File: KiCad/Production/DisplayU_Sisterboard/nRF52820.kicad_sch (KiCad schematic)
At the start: 20 parts, among them X1 32MHz ±40 ppm

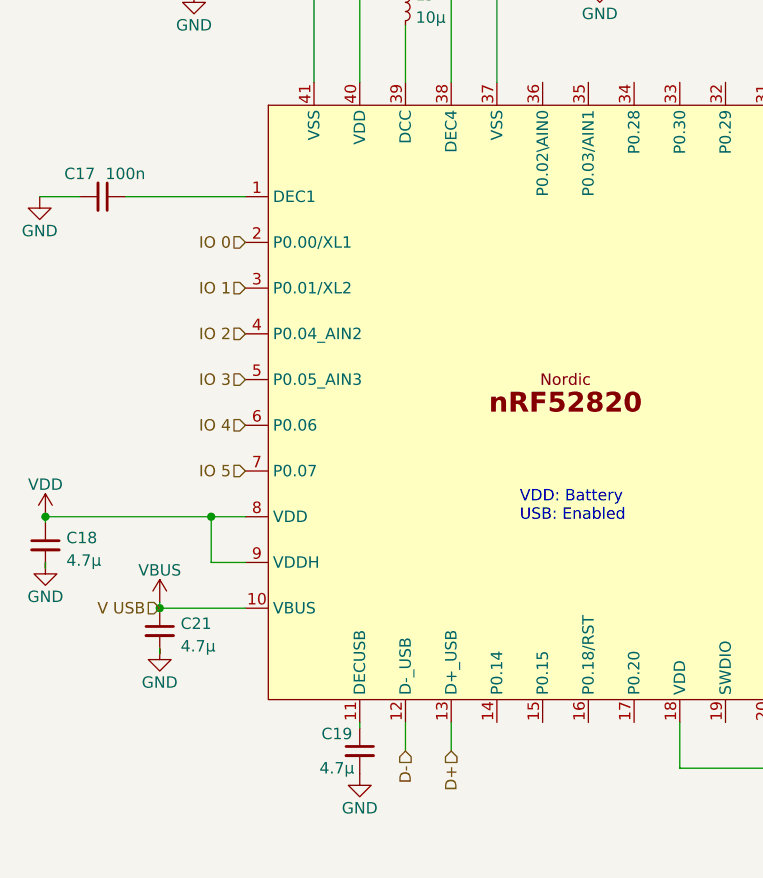
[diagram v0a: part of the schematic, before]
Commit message: Microcontroller integration (almost done)
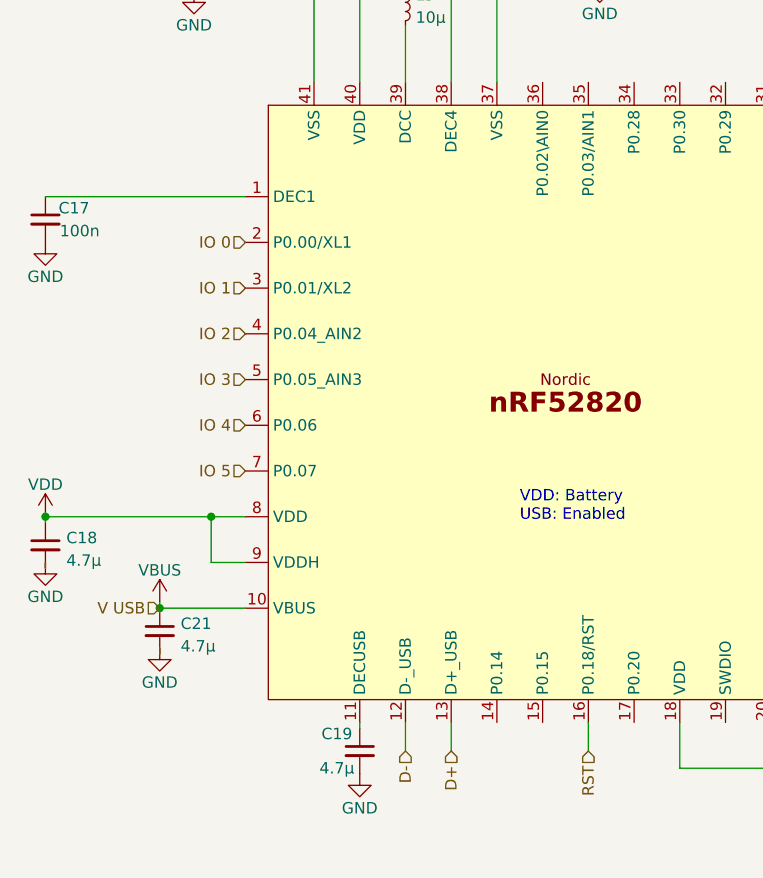
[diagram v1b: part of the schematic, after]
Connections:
- net RST: now reaches U1.16 (P0.18/RST)
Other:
- moved on the sheet: C17
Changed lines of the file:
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@@
     (stroke (width 0) (type default))
   )
-  (wire (pts (xy 124.46 73.66) (xy 111.125 73.66))
+  (wire (pts (xy 124.46 73.66) (xy 102.235 73.66))
     (stroke (width 0) (type default))
   )
@@
     (stroke (width 0) (type default))
   )
+  (wire (pts (xy 162.56 132.08) (xy 162.56 135.255))
+    (stroke (width 0) (type default))
+  )
   (wire (pts (xy 132.08 50.8) (xy 118.745 50.8))
     (stroke (width 0) (type default))
@@
   )
   (wire (pts (xy 114.935 119.38) (xy 114.935 118.745))
-    (stroke (width 0) (type default))
-  )
-  (wire (pts (xy 106.045 73.66) (xy 101.6 73.66))
     (stroke (width 0) (type default))
   )
@@
   )
   (hierarchical_label "D-" (shape input) (at 142.24 135.255 270) (fields_autoplaced)
+    (effects (font (size 1.27 1.27)) (justify right))
+  )
+  (hierarchical_label "RST" (shape input) (at 162.56 135.255 270) (fields_autoplaced)
     (effects (font (size 1.27 1.27)) (justify right))
   )
@@
     )
   )
-  (symbol (lib_id "power:GND") (at 101.6 73.66 0) (unit 1)
-    (in_bom yes) (on_board yes) (dnp no)
-    (property "Reference" "#PWR015" (at 101.6 80.01 0)
-      (effects (font (size 1.27 1.27)) hide)
-    )
-    (property "Value" "GND" (at 101.6 77.47 0)
-      (effects (font (size 1.27 1.27)))
-    )
-    (property "Footprint" "" (at 101.6 73.66 0)
-      (effects (font (size 1.27 1.27)) hide)
-    )
-    (property "Datasheet" "" (at 101.6 73.66 0)
+  (symbol (lib_id "power:GND") (at 102.235 78.74 0) (unit 1)
+    (in_bom yes) (on_board yes) (dnp no)
+    (property "Reference" "#PWR015" (at 102.235 85.09 0)
+      (effects (font (size 1.27 1.27)) hide)
+    )
+    (property "Value" "GND" (at 102.235 82.55 0)
+      (effects (font (size 1.27 1.27)))
+    )
+    (property "Footprint" "" (at 102.235 78.74 0)
+      (effects (font (size 1.27 1.27)) hide)
+    )
+    (property "Datasheet" "" (at 102.235 78.74 0)
       (effects (font (size 1.27 1.27)) hide)
     )
@@
     )
   )
-  (symbol (lib_id "Device:C_Small") (at 108.585 73.66 270) (unit 1)
-    (in_bom yes) (on_board yes) (dnp no)
-    (property "Reference" "C17" (at 106.045 71.12 90)
-      (effects (font (size 1.27 1.27)))
-    )
-    (property "Value" "100n" (at 111.125 71.12 90)
-      (effects (font (size 1.27 1.27)))
-    )
-    (property "Footprint" "" (at 108.585 73.66 0)
-      (effects (font (size 1.27 1.27)) hide)
-    )
-    (property "Datasheet" "~" (at 108.585 73.66 0)
-      (effects (font (size 1.27 1.27)) hide)
-    )
+  (symbol (lib_id "Device:C_Small") (at 102.235 76.2 0) (unit 1)
+    (in_bom yes) (on_board yes) (dnp no)
+    (property "Reference" "C17" (at 105.41 74.93 0)
+      (effects (font (size 1.27 1.27)))
+    )
+    (property "Value" "100n" (at 106.045 77.47 0)
+      (effects (font (size 1.27 1.27)))
+    )
+    (property "Footprint" "" (at 102.235 76.2 0)
+      (effects (font (size 1.27 1.27)) hide)
+    )
+    (property "Datasheet" "~" (at 102.235 76.2 0)
+      (effects (font (size 1.27 1.27)) hide)
+    )

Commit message: Display U is like 99% finished
- BMS Chips prob not needed
- LDO Chip prob not needed
- Final touches
> Start on routing
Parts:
- C1, C15, C16, C17, C18, C19, C2, C20, C21, C3, C4, C5, C6, C7: footprint (none) -> Capacitor_SMD:C_0603_1608Metric
- U1: footprint (none) -> Package_DFN_QFN:QFN-40-1EP_5x5mm_P0.4mm_EP3.8x3.8mm
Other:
- note added: "Datasheet"
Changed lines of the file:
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@@
     (stroke (width 0) (type default))
+  )
+  (text "Datasheet" (at 193.675 67.945 0)
+    (effects (font (size 1.27 1.27)) (justify left bottom) (href "https://infocenter.nordicsemi.com/index.jsp?topic=%2Fps_nrf52820%2Fordering_info.html"))
   )
   (text "VDD: Battery\nUSB: Enabled\n" (at 154.94 109.855 0)
@@
       (effects (font (size 1.27 1.27)))
     )
-    (property "Footprint" "" (at 215.9 88.9 0)
+    (property "Footprint" "Capacitor_SMD:C_0603_1608Metric" (at 215.9 88.9 0)
       (effects (font (size 1.27 1.27)) hide)
     )
@@
       (effects (font (size 1.27 1.27)))
     )
-    (property "Footprint" "" (at 215.9 78.74 0)
+    (property "Footprint" "Capacitor_SMD:C_0603_1608Metric" (at 215.9 78.74 0)
       (effects (font (size 1.27 1.27)) hide)
     )
@@
   )
   (symbol (lib_id "NRF:nRF52820") (at 127 63.5 0) (unit 1)
-    (in_bom yes) (on_board yes) (dnp no) (fields_autoplaced)
-    (property "Reference" "U1" (at 194.7643 69.132 0)
+    (in_bom yes) (on_board yes) (dnp no)
+    (property "Reference" "U1" (at 194.945 64.77 0)
       (effects (font (size 1.27 1.27)))
     )
@@
       (effects (font (size 1.27 1.27)))
     )
-    (property "Footprint" "" (at 127 66.04 0)
+    (property "Footprint" "Package_DFN_QFN:QFN-40-1EP_5x5mm_P0.4mm_EP3.8x3.8mm" (at 127 66.04 0)
       (effects (font (size 1.27 1.27)) hide)
     )
@@
       (effects (font (size 1.27 1.27)) (justify left))
     )
-    (property "Footprint" "" (at 118.745 47.625 0)
+    (property "Footprint" "Capacitor_SMD:C_0603_1608Metric" (at 118.745 47.625 0)
       (effects (font (size 1.27 1.27)) hide)
     )
@@
       (effects (font (size 1.27 1.27)) (justify left))
     )
-    (property "Footprint" "" (at 205.74 139.7 0)
+    (property "Footprint" "Capacitor_SMD:C_0603_1608Metric" (at 205.74 139.7 0)
       (effects (font (size 1.27 1.27)) hide)
     )
@@
       (effects (font (size 1.27 1.27)) (justify left))
     )
-    (property "Footprint" "" (at 114.935 121.92 0)
+    (property "Footprint" "Capacitor_SMD:C_0603_1608Metric" (at 114.935 121.92 0)
       (effects (font (size 1.27 1.27)) hide)
     )
@@
       (effects (font (size 1.27 1.27)) (justify left))
     )
-    (property "Footprint" "" (at 157.48 46.99 0)
+    (property "Footprint" "Capacitor_SMD:C_0603_1608Metric" (at 157.48 46.99 0)
       (effects (font (size 1.27 1.27)) hide)
     )
@@
       (effects (font (size 1.27 1.27)) (justify left))
     )
-    (property "Footprint" "" (at 222.885 64.135 0)
+    (property "Footprint" "Capacitor_SMD:C_0603_1608Metric" (at 222.885 64.135 0)
       (effects (font (size 1.27 1.27)) hide)
     )
@@
       (effects (font (size 1.27 1.27)) hide)
     )
-    (property "Footprint" "" (at 215.9 83.82 0)
+    (property "Footprint" "Capacitor_SMD:C_0603_1608Metric" (at 215.9 83.82 0)
       (effects (font (size 1.27 1.27)) hide)
     )
@@
       (effects (font (size 1.27 1.27)) (justify left))
     )
-    (property "Footprint" "" (at 217.17 106.68 0)
+    (property "Footprint" "Capacitor_SMD:C_0603_1608Metric" (at 217.17 106.68 0)
       (effects (font (size 1.27 1.27)) hide)
     )
@@
       (effects (font (size 1.27 1.27)))
     )
-    (property "Footprint" "" (at 102.235 76.2 0)
+    (property "Footprint" "Capacitor_SMD:C_0603_1608Metric" (at 102.235 76.2 0)
       (effects (font (size 1.27 1.27)) hide)
     )
@@
       (effects (font (size 1.27 1.27)))
     )
-    (property "Footprint" "" (at 137.16 135.255 0)
+    (property "Footprint" "Capacitor_SMD:C_0603_1608Metric" (at 137.16 135.255 0)
       (effects (font (size 1.27 1.27)) hide)
     )
@@
       (effects (font (size 1.27 1.27)) (justify left))
     )
-    (property "Footprint" "" (at 205.105 106.68 0)
+    (property "Footprint" "Capacitor_SMD:C_0603_1608Metric" (at 205.105 106.68 0)
       (effects (font (size 1.27 1.27)) hide)
     )
@@
       (effects (font (size 1.27 1.27)) (justify left))
     )
-    (property "Footprint" "" (at 102.235 112.395 0)
+    (property "Footprint" "Capacitor_SMD:C_0603_1608Metric" (at 102.235 112.395 0)
       (effects (font (size 1.27 1.27)) hide)
     )
@@
       (effects (font (size 1.27 1.27)) (justify left))
     )
-    (property "Footprint" "" (at 163.83 46.99 0)
-      (effects (font (size 1.27 1.27)) hide)
-    )
+    (property "Footprint" "Capacitor_SMD:C_0603_1608Metric" (at 163.83 46.99 0)
+      (effects (font (size 1.27 1.27)) hide)
+    )

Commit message: Schematic is done
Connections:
- net IO 6: now reaches U1.31 (P0.08)
- net D+ renamed DATA+
- net D- renamed DATA-
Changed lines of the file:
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@@
     (effects (font (size 1.27 1.27)) (justify left bottom))
+  )
+  (global_label "DATA+" (shape input) (at 147.32 135.255 270) (fields_autoplaced)
+    (effects (font (size 1.27 1.27)) (justify right))
+    (property "Intersheetrefs" "${INTERSHEET_REFS}" (at 147.32 143.4138 90)
+      (effects (font (size 1.27 1.27)) (justify right) hide)
+    )
+  )
+  (global_label "GND" (shape input) (at 18.415 20.32 0) (fields_autoplaced)
+    (effects (font (size 1.27 1.27)) (justify left))
+    (property "Intersheetrefs" "${INTERSHEET_REFS}" (at 24.9732 20.32 0)
+      (effects (font (size 1.27 1.27)) (justify left) hide)
+    )
+  )
+  (global_label "DATA-" (shape input) (at 142.24 135.255 270) (fields_autoplaced)
+    (effects (font (size 1.27 1.27)) (justify right))
+    (property "Intersheetrefs" "${INTERSHEET_REFS}" (at 142.24 142.9088 90)
+      (effects (font (size 1.27 1.27)) (justify right) hide)
+    )
+  )
+  (global_label "VBUS" (shape input) (at 114.935 119.38 180) (fields_autoplaced)
+    (effects (font (size 1.27 1.27)) (justify right))
+    (property "Intersheetrefs" "${INTERSHEET_REFS}" (at 107.8842 119.38 0)
+      (effects (font (size 1.27 1.27)) (justify right) hide)
+    )
   )
   (hierarchical_label "RF" (shape input) (at 234.95 104.14 0) (fields_autoplaced)
@@
     (effects (font (size 1.27 1.27)) (justify right))
   )
-  (hierarchical_label "D+" (shape input) (at 147.32 135.255 270) (fields_autoplaced)
-    (effects (font (size 1.27 1.27)) (justify right))
-  )
-  (hierarchical_label "GND" (shape input) (at 118.745 50.8 180) (fields_autoplaced)
-    (effects (font (size 1.27 1.27)) (justify right))
-  )
-  (hierarchical_label "V USB" (shape input) (at 114.935 119.38 180) (fields_autoplaced)
-    (effects (font (size 1.27 1.27)) (justify right))
-  )
   (hierarchical_label "IO 2" (shape input) (at 124.46 88.9 180) (fields_autoplaced)
     (effects (font (size 1.27 1.27)) (justify right))
@@
     (effects (font (size 1.27 1.27)) (justify right))
   )
-  (hierarchical_label "D-" (shape input) (at 142.24 135.255 270) (fields_autoplaced)
-    (effects (font (size 1.27 1.27)) (justify right))
+  (hierarchical_label "IO 6" (shape input) (at 182.88 60.96 90) (fields_autoplaced)
+    (effects (font (size 1.27 1.27)) (justify left))
   )
   (hierarchical_label "RST" (shape input) (at 162.56 135.255 270) (fields_autoplaced)
@@
         )
       )
+    )
+  )
+  (symbol (lib_id "power:GND") (at 18.415 20.32 0) (unit 1)
+    (in_bom yes) (on_board yes) (dnp no)
+    (property "Reference" "#PWR049" (at 18.415 26.67 0)
+      (effects (font (size 1.27 1.27)) hide)
+    )
+    (property "Value" "GND" (at 18.415 24.13 0)
+      (effects (font (size 1.27 1.27)))
+    )
+    (property "Footprint" "" (at 18.415 20.32 0)
+      (effects (font (size 1.27 1.27)) hide)
+    )
+    (property "Datasheet" "" (at 18.415 20.32 0)
+      (effects (font (size 1.27 1.27)) hide)
+    )
+    (pin "1")
+    (instances
+      (project "DisplayU_Sisterboard"
+        (path "/19c7c935-33c8-4c59-9a5d-d605e15c31a3/25a7bd83-bec9-4f3f-8272-59937481b0db/21567c23-4b19-440e-b334-053946d84a03"
+          (reference "#PWR049") (unit 1)
+        )
+        (path "/19c7c935-33c8-4c59-9a5d-d605e15c31a3/25a7bd83-bec9-4f3f-8272-59937481b0db"
+          (reference "#PWR026") (unit 1)
+        )
+      )

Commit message: Routing
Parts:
- added F?: 04941.25NRHF, Fuse:Fuse_0603_1608Metric, symbol Device:Fuse
- L1, L2, L3, L4: footprint (none) -> Inductor_SMD:L_0603_1608Metric
- X1: footprint (none) -> Crystal:Crystal_SMD_SeikoEpson_FA128-4Pin_2.0x1.6mm
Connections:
- net VDD: now also F?.2; no longer U1.40 (VDD)
- net X1+: now reaches C6.1, U1.29 (XC2), X1.2
- net X1-: now reaches C7.1, U1.28 (XC1), X1.1
- new net: F?.1, U1.40 (VDD)
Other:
- note added: "Nordic nRFxx Implementation Battery powered + USB -Sam Dilmaghanian"
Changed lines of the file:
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@@
   (junction (at 222.885 60.96) (diameter 0) (color 0 0 0 0)
   )
-  (wire (pts (xy 118.745 44.45) (xy 137.16 44.45))
-    (stroke (width 0) (type default))
-  )
   (wire (pts (xy 205.74 137.16) (xy 205.74 136.525))
     (stroke (width 0) (type default))
@@
     (stroke (width 0) (type default))
   )
+  (wire (pts (xy 137.16 55.372) (xy 137.16 60.96))
+    (stroke (width 0) (type default))
+  )
   (wire (pts (xy 118.745 50.165) (xy 118.745 50.8))
     (stroke (width 0) (type default))
@@
     (stroke (width 0) (type default))
   )
-  (wire (pts (xy 137.16 44.45) (xy 137.16 60.96))
-    (stroke (width 0) (type default))
-  )
   (wire (pts (xy 120.65 114.3) (xy 120.65 109.22))
     (stroke (width 0) (type default))
@@
     (stroke (width 0) (type default))
   )
+  (wire (pts (xy 137.16 44.45) (xy 118.745 44.45))
+    (stroke (width 0) (type default))
+  )
   (wire (pts (xy 195.58 78.74) (xy 197.485 78.74))
     (stroke (width 0) (type default))
@@
     (stroke (width 0) (type default))
   )
+  (wire (pts (xy 137.16 47.752) (xy 137.16 44.45))
+    (stroke (width 0) (type default))
+  )
   (wire (pts (xy 195.58 99.06) (xy 202.565 99.06))
     (stroke (width 0) (type default))
@@
     (stroke (width 0) (type default))
   )
+  (text "Nordic nRFxx Implementation\nBattery powered + USB\n-Sam Dilmaghanian"
+    (at 179.07 173.99 0)
+    (effects (font (size 1.27 1.27)) (justify left bottom))
+  )
   (text "Datasheet" (at 193.675 67.945 0)
-    (effects (font (size 1.27 1.27)) (justify left bottom) (href "https://infocenter.nordicsemi.com/index.jsp?topic=%2Fps_nrf52820%2Fordering_info.html"))
+    (effects (font (size 1.27 1.27)) (justify left bottom) (href "https://infocenter.nordicsemi.com/pdf/nRF52820_PS_v1.3.pdf"))
   )
   (text "VDD: Battery\nUSB: Enabled\n" (at 154.94 109.855 0)
+    (effects (font (size 1.27 1.27)) (justify left bottom))
+  )
+  (label "X1-" (at 206.248 83.82 270) (fields_autoplaced)
+    (effects (font (size 1.27 1.27)) (justify right bottom))
+  )
+  (label "D-" (at 142.24 133.223 270) (fields_autoplaced)
+    (effects (font (size 1.27 1.27)) (justify right bottom))
+  )
+  (label "D+" (at 147.32 133.223 270) (fields_autoplaced)
+    (effects (font (size 1.27 1.27)) (justify right bottom))
+  )
+  (label "X1+" (at 205.867 78.74 0) (fields_autoplaced)
     (effects (font (size 1.27 1.27)) (justify left bottom))
   )
@@
       (effects (font (size 1.27 1.27)) (justify left))
     )
-    (property "Footprint" "" (at 142.24 46.99 0)
+    (property "Footprint" "Inductor_SMD:L_0603_1608Metric" (at 142.24 46.99 0)
       (effects (font (size 1.27 1.27)) hide)
     )
@@
       (effects (font (size 1.27 1.27)) (justify left))
     )
-    (property "Footprint" "" (at 142.24 52.07 0)
+    (property "Footprint" "Inductor_SMD:L_0603_1608Metric" (at 142.24 52.07 0)
       (effects (font (size 1.27 1.27)) hide)
     )
@@
       (effects (font (size 1.27 1.27)) (justify left))
     )
-    (property "Footprint" "" (at 211.455 104.14 0)
+    (property "Footprint" "Inductor_SMD:L_0603_1608Metric" (at 211.455 104.14 0)
       (effects (font (size 1.27 1.27)) hide)
     )
@@
       (effects (font (size 1.27 1.27)) (justify left))
     )
-    (property "Footprint" "" (at 226.06 104.14 0)
+    (property "Footprint" "Inductor_SMD:L_0603_1608Metric" (at 226.06 104.14 0)
       (effects (font (size 1.27 1.27)) hide)
     )
@@
         (path "/19c7c935-33c8-4c59-9a5d-d605e15c31a3/25a7bd83-bec9-4f3f-8272-59937481b0db/21567c23-4b19-440e-b334-053946d84a03"
           (reference "C3") (unit 1)
+        )
+      )
+    )
+  )
+  (symbol (lib_id "Device:Fuse") (at 137.16 51.562 180) (unit 1)
+    (in_bom yes) (on_board yes) (dnp no)
+    (property "Reference" "F?" (at 135.509 47.879 0)
+      (effects (font (size 1.27 1.27)))
+    )
+    (property "Value" "04941.25NRHF" (at 138.938 51.816 90)
+      (effects (font (size 1.27 1.27)))
+    )
+    (property "Footprint" "Fuse:Fuse_0603_1608Metric" (at 138.938 51.562 90)
+      (effects (font (size 1.27 1.27)) hide)
+    )
+    (property "Datasheet" "~" (at 137.16 51.562 0)
+      (effects (font (size 1.27 1.27)) hide)
+    )
+    (pin "1")
+    (pin "2")
+    (instances
+      (project "EBS_Main"
+        (path "/0a240a99-769c-44e4-a1cf-c8ae622a9801/bdd1c018-ef1f-4016-b07d-24e58036b989"
+          (reference "F?") (unit 1)
+        )
+      )
+      (project "DisplayU_Sisterboard"
+        (path "/19c7c935-33c8-4c59-9a5d-d605e15c31a3/bc90aa39-2744-4a84-88b0-6b5f6472e99d"
+          (reference "F4") (unit 1)
+        )
+        (path "/19c7c935-33c8-4c59-9a5d-d605e15c31a3/25a7bd83-bec9-4f3f-8272-59937481b0db"
+          (reference "F1") (unit 1)
+        )
+        (path "/19c7c935-33c8-4c59-9a5d-d605e15c31a3/25a7bd83-bec9-4f3f-8272-59937481b0db/21567c23-4b19-440e-b334-053946d84a03"
+          (reference "F1") (unit 1)
         )
       )
@@
       (effects (font (size 1.27 1.27)) (justify right))
     )
-    (property "Footprint" "" (at 197.485 81.28 0)
-      (effects (font (size 1.27 1.27)) hide)
-    )
+    (property "Footprint" "Crystal:Crystal_SMD_SeikoEpson_FA128-4Pin_2.0x1.6mm" (at 197.485 81.28 0)
+      (effects (font (size 1.27 1.27)) hide)
+    )

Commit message: Berekening/Metingen Verslag
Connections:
- no-connect marks 0 -> 13
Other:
- note added: "nRF52820-CFAA-D-R7"
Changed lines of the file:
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@@
   (junction (at 222.885 60.96) (diameter 0) (color 0 0 0 0)
   )
+  (no_connect (at 172.72 60.96))
+  (no_connect (at 195.58 114.3))
+  (no_connect (at 157.48 60.96))
+  (no_connect (at 157.48 132.08))
+  (no_connect (at 167.64 60.96))
+  (no_connect (at 177.8 60.96))
+  (no_connect (at 162.56 60.96))
+  (no_connect (at 182.88 132.08))
+  (no_connect (at 152.4 132.08))
+  (no_connect (at 177.8 132.08))
+  (no_connect (at 195.58 109.22))
+  (no_connect (at 195.58 119.38))
+  (no_connect (at 167.64 132.08))
   (wire (pts (xy 205.74 137.16) (xy 205.74 136.525))
     (stroke (width 0) (type default))
@@
     (effects (font (size 1.27 1.27)) (justify left bottom))
   )
+  (text "nRF52820-CFAA-D-R7\n" (at 193.675 70.485 0)
+    (effects (font (size 1.27 1.27)) (justify left bottom))
+  )
